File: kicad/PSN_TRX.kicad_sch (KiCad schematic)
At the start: 150 parts, among them IC1 LP2950L-5.0V, IC2 NJM2904, J1 PWR_IN, J2 SP-OUT, J3 RF-IN, J4 MIC-IN, J5 I2C_OUT, J6 Volume, K1 G5V-2, Q1 3SK59, Q11 2SC1815, Q12 2SC1815, Q13 2SC1815, Q14 2SK439, Q15 2SC1815, Q17 2SC1815, Q2 2SC1923, Q3 2SC1815, Q4 2SC1815, Q5 2SC2120, Q6 2SA950, Q9 2SK439, SW1 SW, SW2 SW, T1 ST-71, U1 Si5351_DIP8, U2 AE-LCNV4-MOSFET, U3 LP2950-3.3_TO92

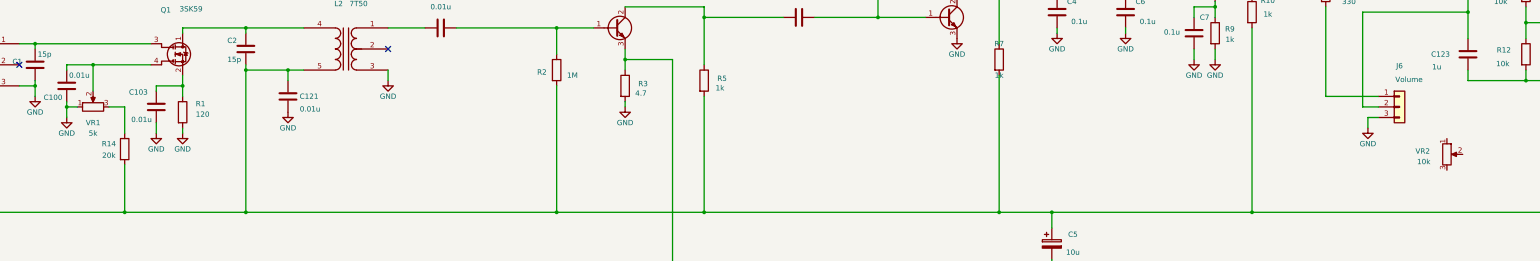
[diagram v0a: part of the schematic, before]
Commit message: fix: VR1/VR2 フットプリントをGF063Pに統一、DNP/NO board設定
- VR1/VR2: Connector_PinHeader → PSN_TRX:Potentiometer_TOCOS_GF063P_Vertical
- VR1/VR2: in_bom/on_board/in_pos_files=no, dnp=yes

Co-Authored-By: Claude Sonnet 4.6 <noreply@anthropic.com>
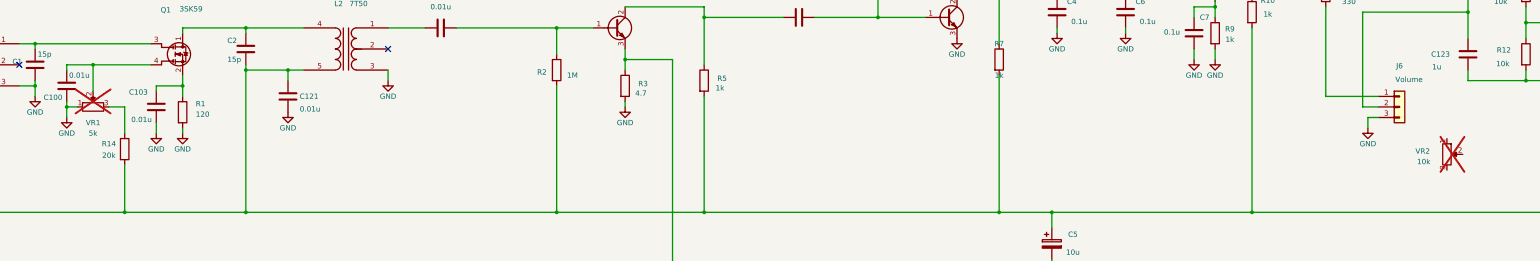
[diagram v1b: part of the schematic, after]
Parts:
- VR1, VR2: footprint Connector_PinHeader_2.54mm:PinHeader_1x03_P2.54mm_Vertical -> PSN_TRX:Potentiometer_TOCOS_GF063P_Vertical; now not fitted; now left out of the parts list
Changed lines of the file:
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@@
 		(body_style 1)
 		(exclude_from_sim no)
-		(in_bom yes)
+		(in_bom no)
 		(on_board no)
-		(in_pos_files yes)
-		(dnp no)
+		(in_pos_files no)
+		(dnp yes)
 		(property "Reference" "VR2"
 			(at 514.858 147.828 0)
@@
 			)
 		)
-		(property "Footprint" "Connector_PinHeader_2.54mm:PinHeader_1x03_P2.54mm_Vertical"
+		(property "Footprint" "PSN_TRX:Potentiometer_TOCOS_GF063P_Vertical"
 			(at 520.7 148.59 0)
 			(hide yes)
@@
 		(body_style 1)
 		(exclude_from_sim no)
-		(in_bom yes)
+		(in_bom no)
 		(on_board no)
-		(in_pos_files yes)
-		(dnp no)
+		(in_pos_files no)
+		(dnp yes)
 		(fields_autoplaced yes)
 		(property "Reference" "VR1"
@@
 			)
 		)
-		(property "Footprint" "Connector_PinHeader_2.54mm:PinHeader_1x03_P2.54mm_Vertical"
+		(property "Footprint" "PSN_TRX:Potentiometer_TOCOS_GF063P_Vertical"
 			(at 194.31 137.16 0)
 			(hide yes)

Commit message: feat: GF063Pポテンショメータのカスタムシンボル追加・フットプリント修正、VR3-7をPSN_TRXライブラリに移行
- PSN_TRX:Potentiometer_GF063P シンボルをシンボルライブラリに追加（VRプレフィックス、フットプリント紐付け済み）
- Potentiometer_TOCOS_GF063P_Vertical フットプリントのピン配置をデータシートに基づき修正
  - 旧: ピン1・2・3が一直線（誤り）
  - 新: 三角配置（ピン2ワイパーを2.5mm上方にオフセット）
- VR3〜VR7のシンボル参照を Device:R_Potentiometer → PSN_TRX:Potentiometer_GF063P に変更

Co-Authored-By: Claude Sonnet 4.6 <noreply@anthropic.com>
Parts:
- removed VR3: 10k, PSN_TRX:Potentiometer_TOCOS_GF063P_Vertical, symbol Device:R_Potentiometer
- removed VR4, VR5: 1k, PSN_TRX:Potentiometer_TOCOS_GF063P_Vertical, symbol Device:R_Potentiometer
- removed VR6, VR7: 500, PSN_TRX:Potentiometer_TOCOS_GF063P_Vertical, symbol Device:R_Potentiometer
- added C8b2: 10u, Capacitor_THT:CP_Radial_D5.0mm_P2.00mm, symbol Device:C_Polarized
- added J7: Volume, Connector_PinHeader_2.54mm:PinHeader_1x03_P2.54mm_Vertical, symbol Connector_Generic:Conn_01x03
- added VR3: 10k, PSN_TRX:Potentiometer_TOCOS_GF063P_Vertical, symbol PSN_TRX:Potentiometer_GF063P
- added VR4, VR5: 1k, PSN_TRX:Potentiometer_TOCOS_GF063P_Vertical, symbol PSN_TRX:Potentiometer_GF063P
- added VR6, VR7: 500, PSN_TRX:Potentiometer_TOCOS_GF063P_Vertical, symbol PSN_TRX:Potentiometer_GF063P
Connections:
- net +5V: now also U3.3 (VI)
- net GND: now also U3.2 (GND), C8b2.2, J7.3 (Pin_3); no longer VR1.1
- net at C129.2, L16.2: now also VR6.2, VR6.3
- net at C168.1, IC2.2 (-): now also VR3.1
- net at C22.1, R34.1: now also VR7.1
- net at C100.1, Q1.4 (G2): now also J7.2 (Pin_2); no longer VR1.2
- net at VR1.3: no longer R14.1
- net at C22.2, L10.1: now also VR5.2
- net at C130.2, L17.2: now also VR7.2, VR7.3
- net at C114.2, C21.1, R21.1: now also VR6.1
- net at C21.2, L9.1: now also VR4.2
- net at D1.1 (K): now also VR4.1
- net at C164.1, R26.2: now also VR3.2, VR3.3
- net at D3.1 (K): now also VR5.1
- net at D4.2 (A): now also VR5.3
- net at A1.16 (3.3V), U1.8 (VDD), U2.9 (LV): now also U3.1 (VO), C8b2.1
- net at D2.2 (A): now also VR4.3
- new net: J7.1 (Pin_1), R14.1
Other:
- moved on the sheet: C100, C103, R14, U3, VR1

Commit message: feat: J8ロータリーエンコーダ用4ピンコネクタを回路図に追加
Conn_01x04: ENC_A(D0), ENC_B(D1), ENC_SW(D2), GND

Co-Authored-By: Claude Sonnet 4.6 <noreply@anthropic.com>
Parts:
- removed A1: Arduino_Nano_R4_Socket, PSN_TRX:Arduino_Nano_R4_Socket, symbol PSN_TRX:Arduino_Nano_R4_Socket
- removed U2: AE-LCNV4-MOSFET, PSN_TRX:DIP-12_W7.62mm, symbol PSN_TRX:AE-LCNV4-MOSFET
- added A2: Seeeduino_XIAO_Socket, PSN_TRX:Seeeduino_XIAO_Socket, symbol PSN_TRX:Seeeduino_XIAO_Socket
- added C14, C16: 100pF, Capacitor_THT:C_Disc_D5.0mm_W2.5mm_P5.00mm, symbol Device:C
- added C15: 22pF, Capacitor_THT:C_Disc_D5.0mm_W2.5mm_P5.00mm, symbol Device:C
- added Cbp3: 1000pF, Capacitor_THT:C_Disc_D5.0mm_W2.5mm_P5.00mm, symbol Device:C
- added Cbp4: 0.1uF, Capacitor_THT:C_Disc_D5.0mm_W2.5mm_P5.00mm, symbol Device:C
- added D10, D9: 1N4148, Diode_THT:D_DO-35_SOD27_P7.62mm_Horizontal, symbol Device:D
- added J8: Volume, Connector_PinHeader_2.54mm:PinHeader_1x03_P2.54mm_Vertical, symbol Connector_Generic:Conn_01x03
- added J8: Rotary_Encoder, Connector_PinHeader_2.54mm:PinHeader_1x04_P2.54mm_Vertical, symbol Connector_Generic:Conn_01x04
- added L5: 47nH, Inductor_THT:L_Axial_L9.0mm_D4.0mm_P12.5mm_Horizontal_RM12.5mm, symbol Device:L
- added Q18: 2SC1971, Package_TO_SOT_THT:TO-220-3_Vertical, symbol Transistor_BJT:Q_NPN_BCE
- added R19, R20: 10, Resistor_THT:R_Axial_DIN0207_L6.3mm_D2.5mm_P10.16mm_Horizontal, symbol Device:R
- added R37: 470, Resistor_THT:R_Axial_DIN0207_L6.3mm_D2.5mm_P10.16mm_Horizontal, symbol Device:R
- added RFC2: 10uH, Inductor_THT:L_Axial_L9.0mm_D4.0mm_P12.5mm_Horizontal_RM12.5mm, symbol Device:L
- added VR9: 500, Potentiometer_THT:Potentiometer_Bourns_3266W_Vertical, symbol Device:R_Potentiometer
- J1: value PWR_IN -> RF_IN
- J3: value RF-IN -> PWR_IN
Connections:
- net GND: now also C15.2, Cbp3.2, Cbp4.2, D10.2 (A), R19.2; no longer U3.2 (GND)
- net TX_+12V: now reaches C118.1, C126.1, C24.2, C31.2, K1.9, L12.3 (SB), L13.3 (SB), LED2.2 (A), R22.1, R24.1, R29.1, R32.1, R35.1, R40.2
- net TX_+12V: now also Cbp3.1, Cbp4.1, RFC2.1
- net at L14.2: now also C14.2; no longer L13.4 (AA)
- net at C8b2.1, U1.8 (VDD), U3.1 (VO): now also A2.8 (VIN)
- net at J5.1 (SDA), U1.3 (SDA): now also A2.5 (D4/SDA)
- net at J5.2 (SCL), U1.2 (SCL): now also A2.6 (D5/SCL)
- new net: C15.1, L5.2, Q18.1 (B), R20.1
- new net: C14.1, Q18.2 (C), RFC2.2
- new net: Q18.3 (E), R19.1
- new net: D9.1 (K), VR9.3
- new net: D10.1 (K), D9.2 (A)
- new net: R20.2, VR9.2
- new net: R37.2, VR9.1
- new net: C16.2, L5.1
- new net: C16.1, L13.4 (AA)
- new net TX+12V: R37.1
- no-connect marks 33 -> 9
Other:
- moved on the sheet: C117, C118, C119, C120, C124, C125, C126, C21, C22, C23, C24, C31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

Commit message: fix: J8を3ピン(Conn_01x03)から4ピン(Conn_01x04)に変更、重複エントリを削除
Co-Authored-By: Claude Sonnet 4.6 <noreply@anthropic.com>
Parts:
- removed J8: Rotary_Encoder, Connector_PinHeader_2.54mm:PinHeader_1x04_P2.54mm_Vertical, symbol Connector_Generic:Conn_01x04
- J8: footprint Connector_PinHeader_2.54mm:PinHeader_1x03_P2.54mm_Vertical -> Connector_PinHeader_2.54mm:PinHeader_1x04_P2.54mm_Vertical; symbol Connector_Generic:Conn_01x03 -> Connector_Generic:Conn_01x04
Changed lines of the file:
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@@
 	)
 	(symbol
-		(lib_id "Connector_Generic:Conn_01x03")
+		(lib_id "Connector_Generic:Conn_01x04")
 		(at 775.97 312.42 0)
 		(unit 1)
@@
 			)
 		)
-		(property "Footprint" "Connector_PinHeader_2.54mm:PinHeader_1x03_P2.54mm_Vertical"
+		(property "Footprint" "Connector_PinHeader_2.54mm:PinHeader_1x04_P2.54mm_Vertical"
 			(at 775.97 312.42 0)
 			(hide yes)
@@
 			)
 		)
-		(property "Description" "Generic connector, single row, 01x03, script generated (kicad-library-utils/schlib/autogen/connector/)"
+		(property "Description" "Generic connector, single row, 01x04"
 			(at 775.97 312.42 0)
 			(hide yes)
@@
 		(pin "3"
 		)
+		(pin "4"
+		)
 		(instances
 			(project "PSN_TRX"
@@
 					(unit 1)
 				)
-			)
-		)
-	)
-	(symbol
-		(lib_id "Connector_Generic:Conn_01x04")
-		(at 200.66 153.67 0)
-		(mirror y)
-		(unit 1)
-		(body_style 1)
-		(exclude_from_sim no)
-		(in_bom yes)
-		(on_board yes)
-		(in_pos_files yes)
-		(dnp no)
-		(property "Reference" "J8"
-			(at 204.216 145.796 0)
-			(show_name no)
-			(do_not_autoplace no)
-			(effects
-				(font
-					(size 1.27 1.27)
-				)
-			)
-		)
-		(property "Value" "Rotary_Encoder"
-			(at 198.374 145.796 0)
-			(show_name no)
-			(do_not_autoplace no)
-			(effects
-				(font
-					(size 1.27 1.27)
-				)
-			)
-		)
-		(property "Footprint" "Connector_PinHeader_2.54mm:PinHeader_1x04_P2.54mm_Vertical"
-			(at 200.66 153.67 0)
-			(hide yes)
-			(show_name no)
-			(do_not_autoplace no)
-			(effects
-				(font
-					(size 1.27 1.27)
-				)
-			)
-		)
-		(property "Datasheet" ""
-			(at 200.66 153.67 0)
-			(hide yes)
-			(show_name no)
-			(do_not_autoplace no)
-			(effects
-				(font
-					(size 1.27 1.27)
-				)
-			)
-		)
-		(property "Description" "Rotary Encoder: ENC_A(D0), ENC_B(D1), ENC_SW(D2), GND"
-			(at 200.66 153.67 0)
-			(hide yes)
-			(show_name no)
-			(do_not_autoplace no)
-			(effects
-				(font
-					(size 1.27 1.27)
-				)
-			)
-		)
-		(pin "1"
-		)
-		(pin "2"
-		)
-		(pin "3"
-		)
-		(pin "4"
-		)
-		(instances
-			(project "PSN_TRX"
-				(path "/50835569-93ad-4c8c-aafc-424a6a3761ef"
-					(reference "J8")
-					(unit 1)
-				)

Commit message: chore: PSN_TRX.net（ネットリスト）を削除
Co-Authored-By: Claude Sonnet 4.6 <noreply@anthropic.com>
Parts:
- J8: value Volume -> Conn_01x04; footprint Connector_PinHeader_2.54mm:PinHeader_1x04_P2.54mm_Vertical -> (none)
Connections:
- net TX_+12V is gone; now on net TX+12V: C118.1, C126.1, C24.2, C31.2, Cbp3.1, Cbp4.1, K1.9, L12.3 (SB), L13.3 (SB), LED2.2 (A), R22.1, R24.1, R29.1, R32.1, R35.1, R40.2, RFC2.1
- net +5V: now also A2.8 (VIN); no longer K1.1
- net +9V: no longer SW1.1 (A)
- net GND: now also A2.9 (GND), J8.4 (Pin_4)
- net at C8b2.1, U1.8 (VDD), U3.1 (VO): no longer A2.8 (VIN)
- net +12V: now reaches J3.1 (Pin_1), K1.13
- net +12V: now also K1.1, SW1.1 (A)
- net at A2.1 (D0/A0): now also J8.1 (Pin_1)
- net at A2.2 (D1/A1): now also J8.2 (Pin_2)
- net at A2.3 (D2/A2): now also J8.3 (Pin_3)
- no-connect marks 9 -> 7

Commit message: refactor: 回路図の部品番号を全タイプ1から連番に振り直し
位置座標(上→下/左→右)でソートして各タイプを1から採番
A,C,D,IC,J,K,L,LED,Q,R,RFC,SW,T,TC,U,VR 全16タイプ 149件更新

Co-Authored-By: Claude Sonnet 4.6 <noreply@anthropic.com>
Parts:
- renumbered A2 to A1, C105 to C1, C123 to C10, C28 to C11, C1 to C12, C100 to C13, C121 to C14, C103 to C15, C30 to C16, C5 to C17, C8 to C18, C8b1 to C19, C104 to C2, C8b2 to C20, C3 to C21, C17 to C22, C113 to C23, C114 to C24, C111 to C25, Cbp3 to C26, Cbp4 to C27, C14 to C28, C16 to C29, C4 to C3, C31 to C30, C15 to C31, C126 to C32, C119 to C33, C24 to C34, C125 to C35, C118 to C36, C23 to C37, C21 to C38, C115 to C39, C6 to C4, C117 to C40, C129 to C41, C128 to C42, C32 to C43, C22 to C44, C116 to C45, C130 to C46, C131 to C47, C124 to C48, C120 to C49, C122 to C5, C167 to C50, C164 to C51, C162 to C52, C159 to C53, C158 to C54, C168 to C55, C163 to C56, C161 to C57, C160 to C58, C166 to C59, C2 to C6, C165 to C60, C101 to C7, C102 to C8, C7 to C9, D9 to D3, D10 to D4, D3 to D5, D7 to D6, D4 to D7, J6 to J4, J7 to J5, J8 to J6, J5 to J7, J4 to J8, L2 to L1, L16 to L10, L17 to L11, L10 to L12, L9 to L13, L8 to L14, L1 to L2, L6 to L3, L15 to L4, L14 to L5, L5 to L6, L13 to L7, L12 to L8, L11 to L9, Q5 to Q1, Q14 to Q10, Q15 to Q11, Q13 to Q12, Q11 to Q13, Q17 to Q14, Q4 to Q2, Q1 to Q3, Q2 to Q4, Q3 to Q5, Q9 to Q7, Q18 to Q8, Q12 to Q9, R8 to R1, R3 to R10, R5 to R11, R7 to R12, R1 to R13, R15 to R14, R14 to R15, R13 to R16, R42 to R17, R51 to R18, R35 to R19, R6 to R2, R19 to R20, R20 to R21, R37 to R22, R39 to R23, R38 to R24, R40 to R25, R36 to R26, R21 to R27, R41 to R28, R34 to R29, R4 to R3, R29 to R30, R27 to R31, R24 to R32, R28 to R33, R26 to R34, R23 to R35, R22 to R36, R30 to R37, R32 to R38, R25 to R39, R10 to R4, R31 to R40, R33 to R41, R43 to R5, R11 to R6, R9 to R7, R12 to R8, R2 to R9, RFC2 to RFC1, SW2 to SW1, SW1 to SW2, TC3 to TC1, U3 to U1, U1 to U2, VR9 to VR3, VR6 to VR5, VR5 to VR6, VR3 to VR8
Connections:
- net GND: now also U1.2 (GND)
- net +12V: no longer names the net of J3.1 (Pin_1), K1.13
- net +12V: no longer K1.1, SW2.1 (A)
- net TX+12V: no longer names the net of C26.1, C27.1, C30.2, C32.1, C34.2, C36.1, K1.9, L7.3 (SB), L8.3 (SB), LED2.2 (A), R19.1, R22.1, R25.2, R30.1, R32.1, R36.1, R38.1, RFC1.1
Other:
- moved on the sheet: D3, D4, R22, VR3

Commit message: fix: RFC1・L6のフットプリントをKiCad 10対応名に更新
L_Axial_L9.0mm_D4.0mm_P12.5mm_Horizontal_RM12.5mm
  → L_Axial_L9.5mm_D4.0mm_P12.70mm_Horizontal_Fastron_SMCC

Co-Authored-By: Claude Sonnet 4.6 <noreply@anthropic.com>
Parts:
- L6, RFC1: footprint Inductor_THT:L_Axial_L9.0mm_D4.0mm_P12.5mm_Horizontal_RM12.5mm -> Inductor_THT:L_Axial_L9.5mm_D4.0mm_P12.70mm_Horizontal_Fastron_SMCC
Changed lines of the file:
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@@
 			)
 		)
-		(property "Footprint" "Inductor_THT:L_Axial_L9.0mm_D4.0mm_P12.5mm_Horizontal_RM12.5mm"
+		(property "Footprint" "Inductor_THT:L_Axial_L9.5mm_D4.0mm_P12.70mm_Horizontal_Fastron_SMCC"
 			(at 229.87 293.37 0)
 			(hide yes)
@@
 			)
 		)
-		(property "Footprint" "Inductor_THT:L_Axial_L9.0mm_D4.0mm_P12.5mm_Horizontal_RM12.5mm"
+		(property "Footprint" "Inductor_THT:L_Axial_L9.5mm_D4.0mm_P12.70mm_Horizontal_Fastron_SMCC"
 			(at 267.97 308.61 0)
 			(hide yes)
